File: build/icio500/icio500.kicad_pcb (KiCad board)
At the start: 4 copper layers, 150.8 x 114.3 mm, 56 parts, among them J1 ?, U1 ?, U2 ?, U3 ?, U4 ?, U5 ?, U6 ?

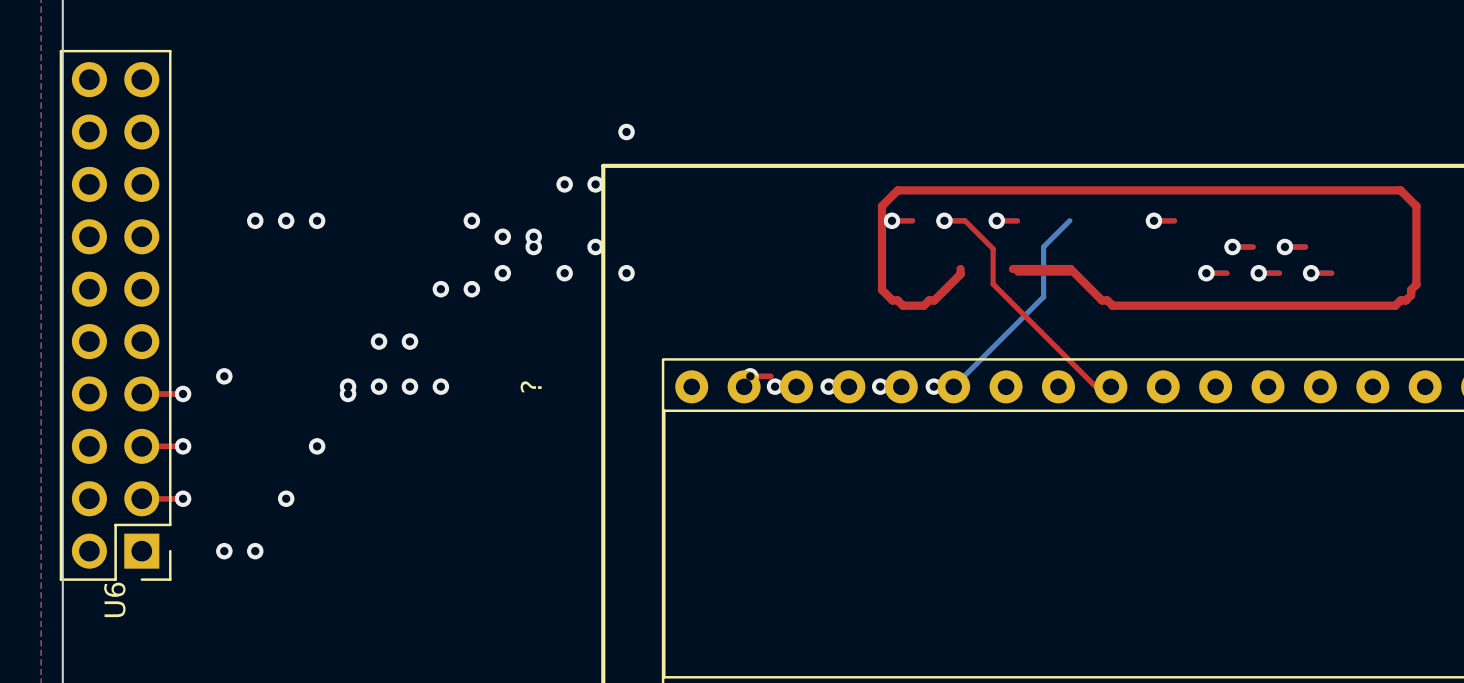
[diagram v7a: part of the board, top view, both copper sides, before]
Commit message: Fix 3D orientation (Ry=90) and completely rewrite U6 routing to minimize vias (4 signal vias)
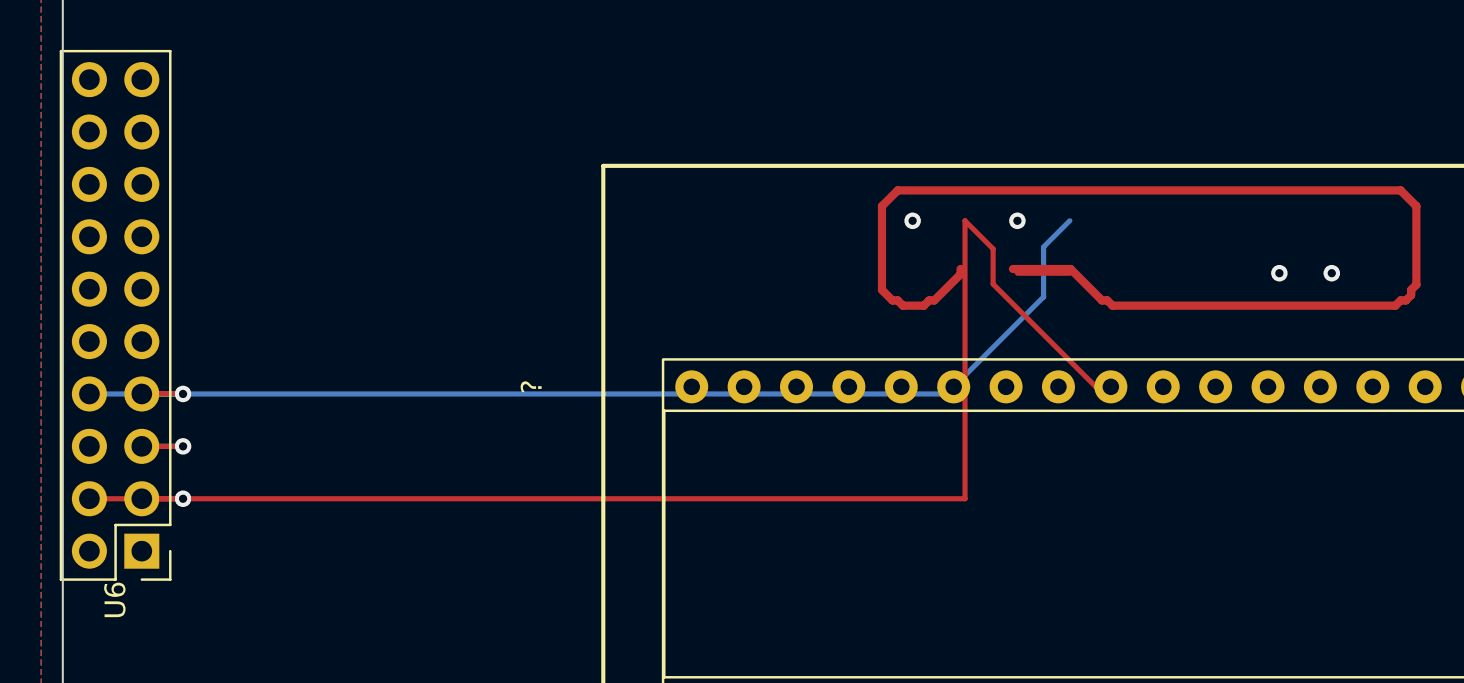
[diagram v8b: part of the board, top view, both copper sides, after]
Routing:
- net gpio_disp_dc: track 76.4 -> 73.4 mm, vias 3 -> 0
- net spi1_mosi: track 67.8 -> 64.8 mm, vias 3 -> 0
- net spi1_miso: track 63.7 -> 60.7 mm, vias 3 -> 0
- net i2c1_sda: track 70.3 -> 67.3 mm, vias 3 -> 0
- net i2c1_scl: track 74.9 -> 71.9 mm, vias 3 -> 1
- net gpio_enc_sw: track 60.0 -> 57.0 mm, vias 3 -> 0
- net gpio_disp_res: track 76.9 -> 73.9 mm, vias 3 -> 1
- net daisy_5v_power: track 155.1 -> 152.1 mm, vias 3 -> 0
- net d14: track 56.4 -> 53.4 mm, vias 3 -> 0
- net d13: track 55.7 -> 52.7 mm, vias 3 -> 0
- net audio_in_r: track 108.5 -> 106.6 mm, vias 3 -> 1
- net spi1_cs: track 69.8 -> 68.2 mm, vias 3 -> 1
- net spi1_sck: track 69.8 -> 68.3 mm, vias 3 -> 0
- net gpio_enc_b: track 59.1 -> 57.8 mm, vias 3 -> 0
